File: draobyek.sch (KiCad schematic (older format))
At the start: 5 parts

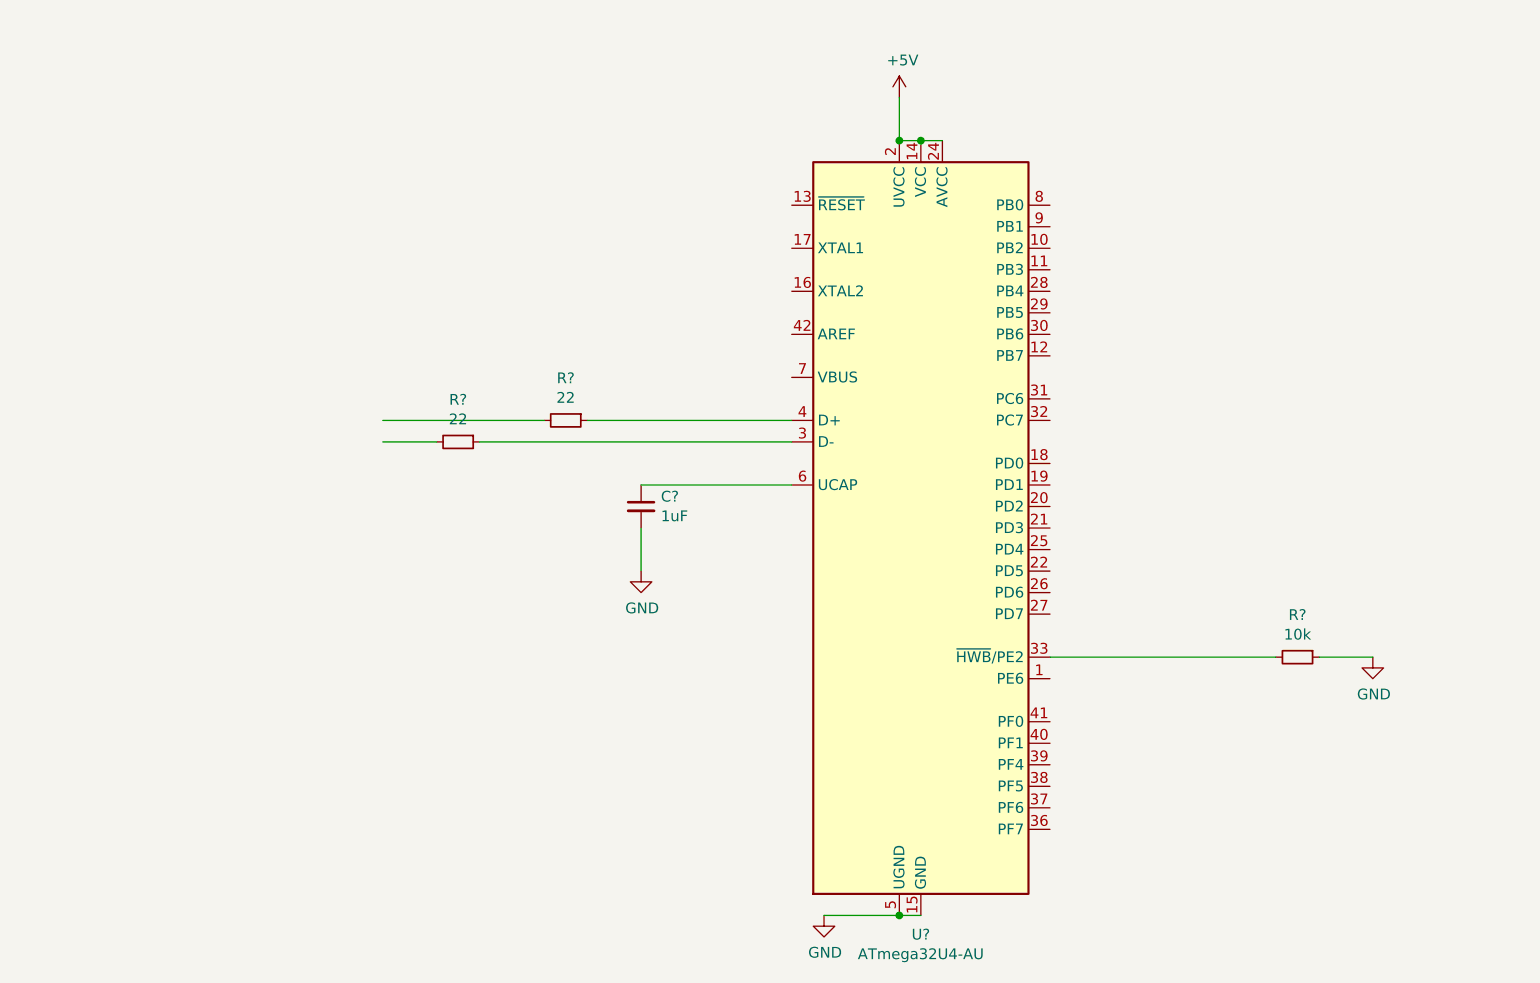
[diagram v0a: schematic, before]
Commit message: Add submodules
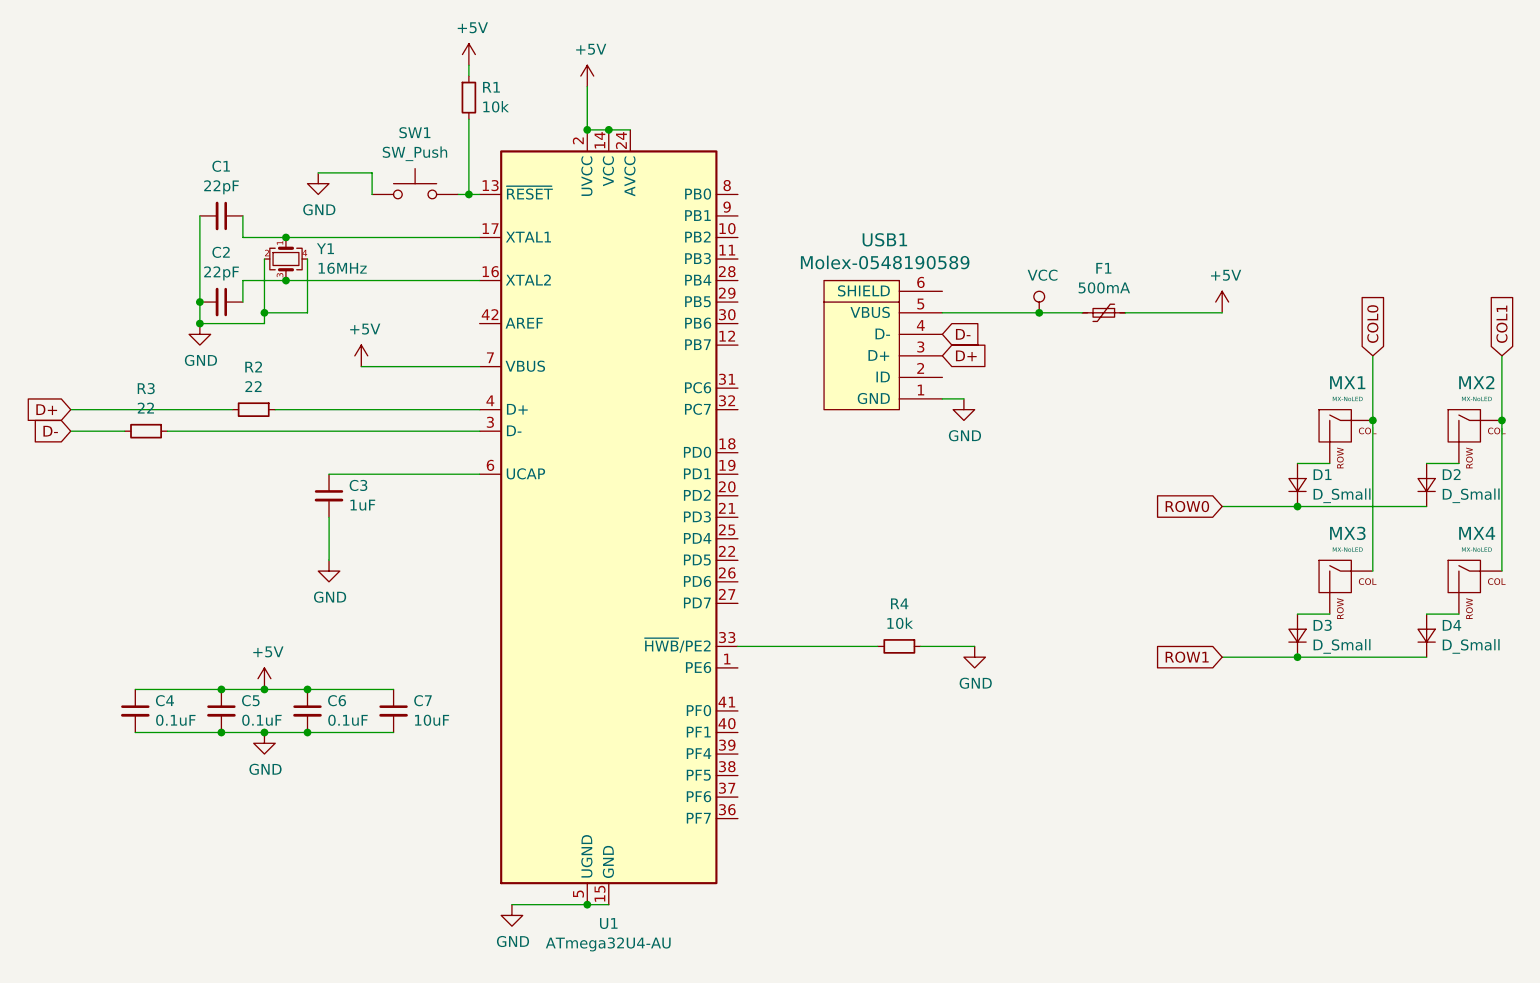
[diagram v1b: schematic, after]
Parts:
- added C1, C2: 22pF, Capacitor_SMD:C_0805_2012Metric, symbol Device:C_Small
- added C4, C5, C6: 0.1uF, Capacitor_SMD:C_0805_2012Metric, symbol Device:C_Small
- added C7: 10uF, Capacitor_SMD:C_0805_2012Metric, symbol Device:C_Small
- added D1, D2, D3, D4: D_Small, Diode_SMD:D_SOD-123, symbol Device:D_Small
- added F1: 500mA, Fuse:Fuse_1206_3216Metric, symbol Device:Polyfuse_Small
- added MX1, MX2, MX3, MX4: MX-NoLED, MX_Alps_Hybrid:MX-1U, symbol MX_Alps_Hybrid:MX-NoLED
- added R1: 10k, Resistor_SMD:R_0805_2012Metric, symbol Device:R_Small
- added SW1: SW_Push, random-keyboard-parts:SKQG-1155865, symbol Switch:SW_Push
- added USB1: Molex-0548190589, random-keyboard-parts:Molex-0548190589, symbol random-keyboard-parts:Molex-0548190589
- added Y1: 16MHz, Crystal:Crystal_SMD_3225-4Pin_3.2x2.5mm, symbol Device:Crystal_GND24_Small
- C3: renamed from C?; footprint (none) -> Capacitor_SMD:C_0805_2012Metric
- R2, R3, R4: renamed from R?; footprint (none) -> Resistor_SMD:R_0805_2012Metric
- gave numbers to parts that had none: 1
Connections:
- net labels added: COL0, COL1, D+, D-, ROW0, ROW1, VCC
- wire segments 13 -> 57
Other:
- moved on the sheet: C3, R2, R3, R4, U1
